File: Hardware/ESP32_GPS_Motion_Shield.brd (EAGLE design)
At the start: 25.4 x 50.8 mm, 38 parts, among them J2 MICRO-SD_CARD_SOCKET, J6 3-PIN SMD, U1 LSM9DS1

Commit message: Double checked layout vs. fixed proto.  Adjusted small shapes.
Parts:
- moved LOGO2 1.80 mm to (7.30, 19.7)
- moved R3 0.16 mm to (10.0, 30.7)
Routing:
- net GPS_LED: track 13.2 -> 13.0 mm, vias 1 -> 0
- net GND: vias 34 -> 36
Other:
- board text removed: "Motion Shield"

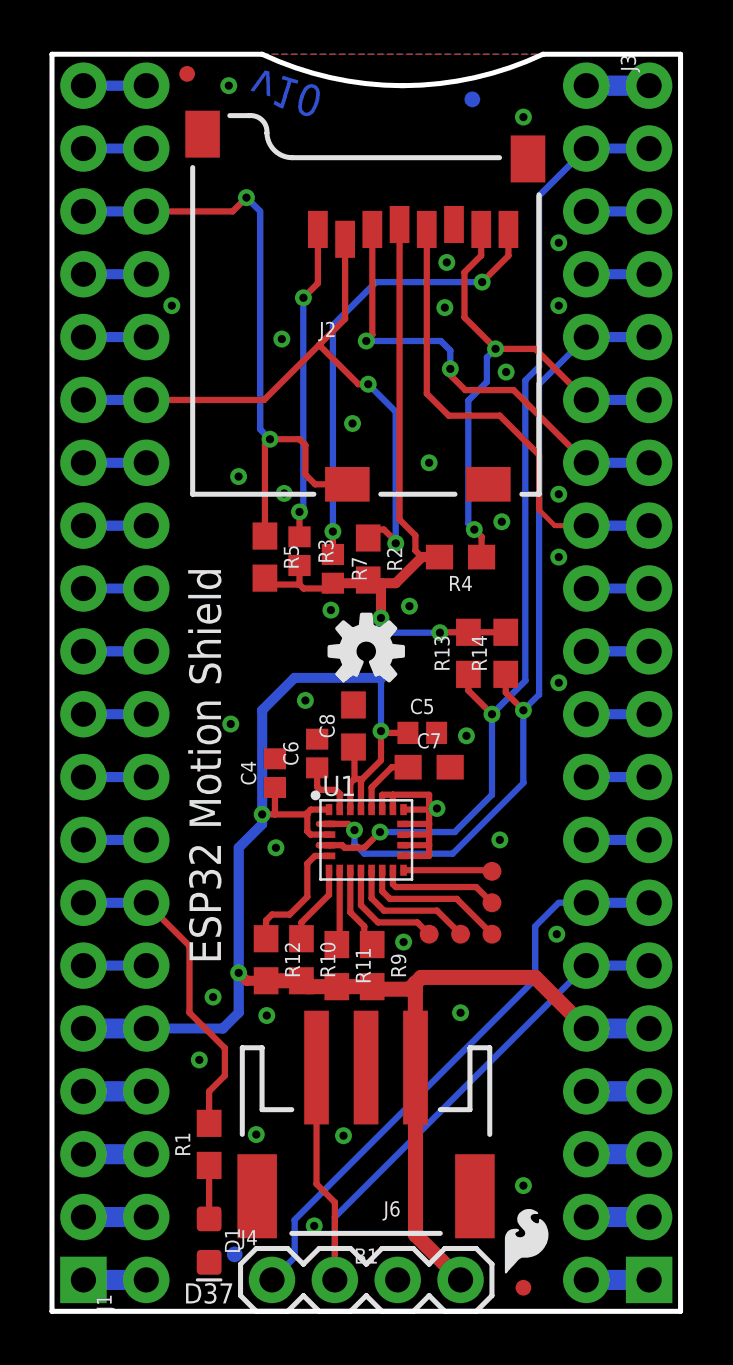
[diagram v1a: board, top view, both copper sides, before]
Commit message: Fixed items from redboard review
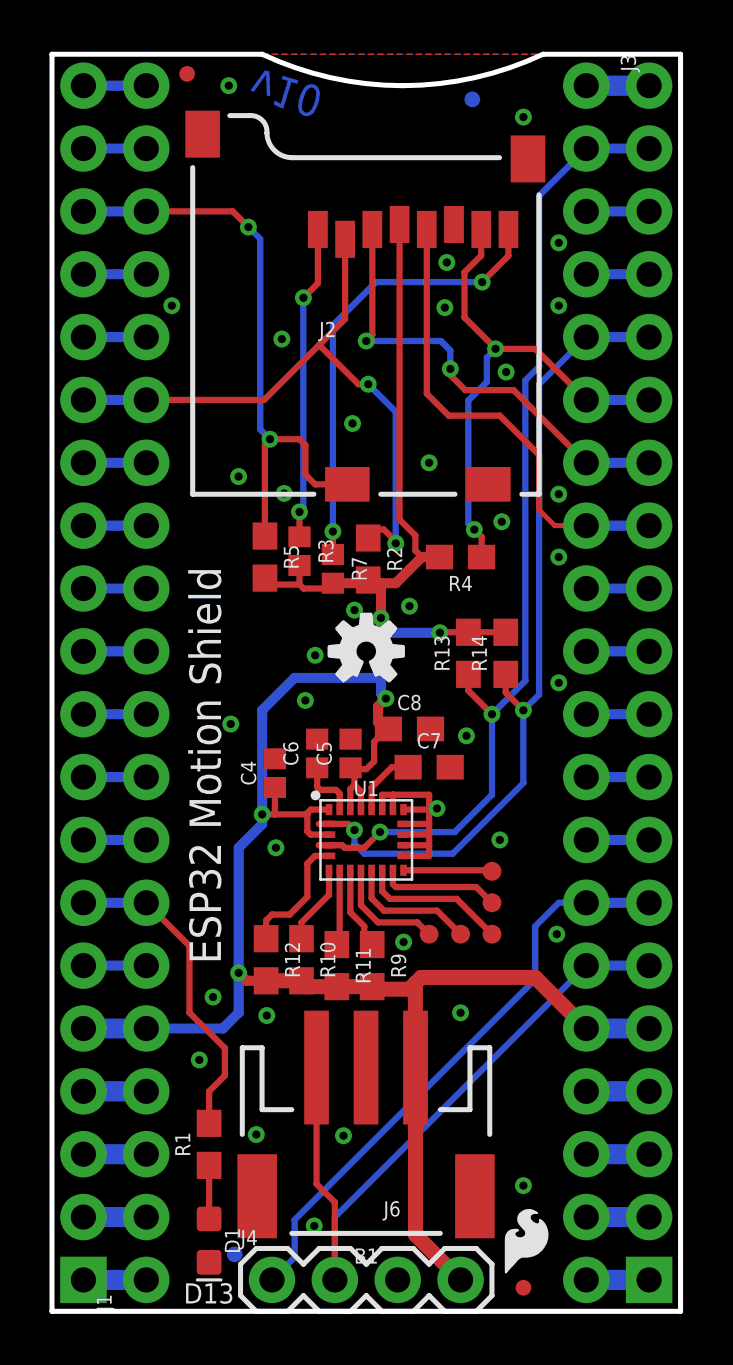
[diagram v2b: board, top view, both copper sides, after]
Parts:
- U1: device LSM9DS1_temp:LGA24-8X4 -> SparkFun-Sensors:LGA-24-3.5X3
- moved C5 3.01 mm to (12.1, 22.5), turned to 90 degrees
- moved C8 2.27 mm to (14.4, 23.5), turned to 0 degrees
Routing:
- net 3.3V: track 104.0 -> 101.8 mm
- net SD_CD: track 25.6 -> 24.4 mm
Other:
- board text added: "D13"
- board text removed: "D37"
